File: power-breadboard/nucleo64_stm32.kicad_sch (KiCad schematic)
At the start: 29 parts, among them U5 STM32G474RBT6

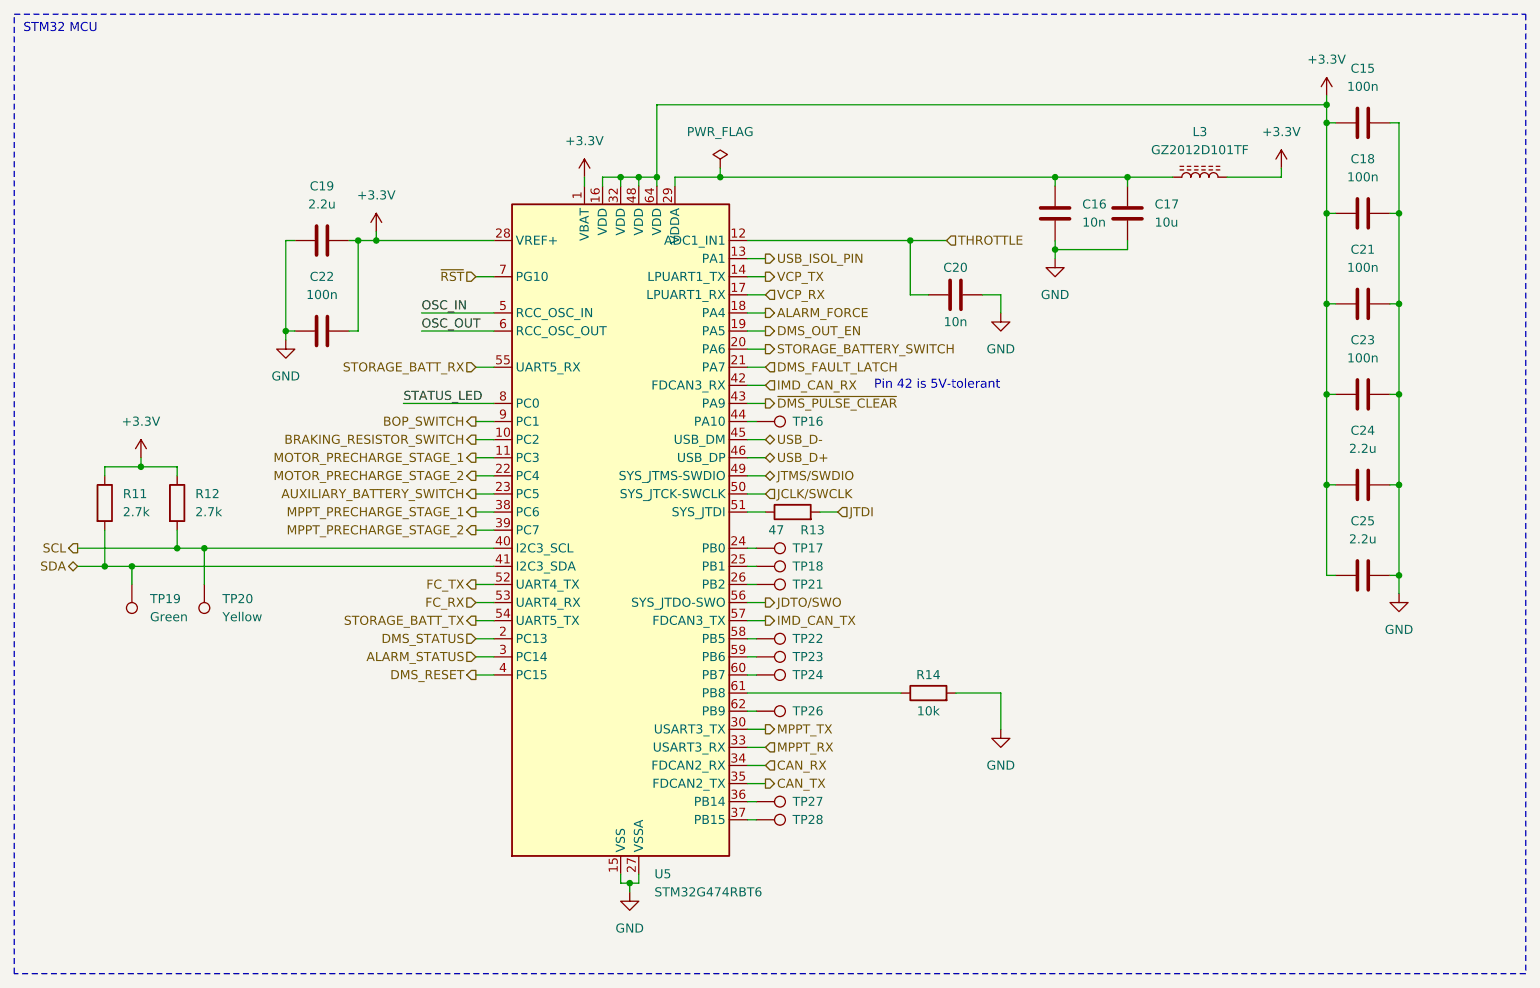
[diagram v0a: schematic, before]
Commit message: power-breadboard: add nucleo pinout connections
- Replace the schematic page with STM32 microcontroller connections.
- Update the date on all pages and some page names
- Add CN10/CN7 connectors, with the CN7 being connected through the
  T-cobbler
- Add peripheral assignation table
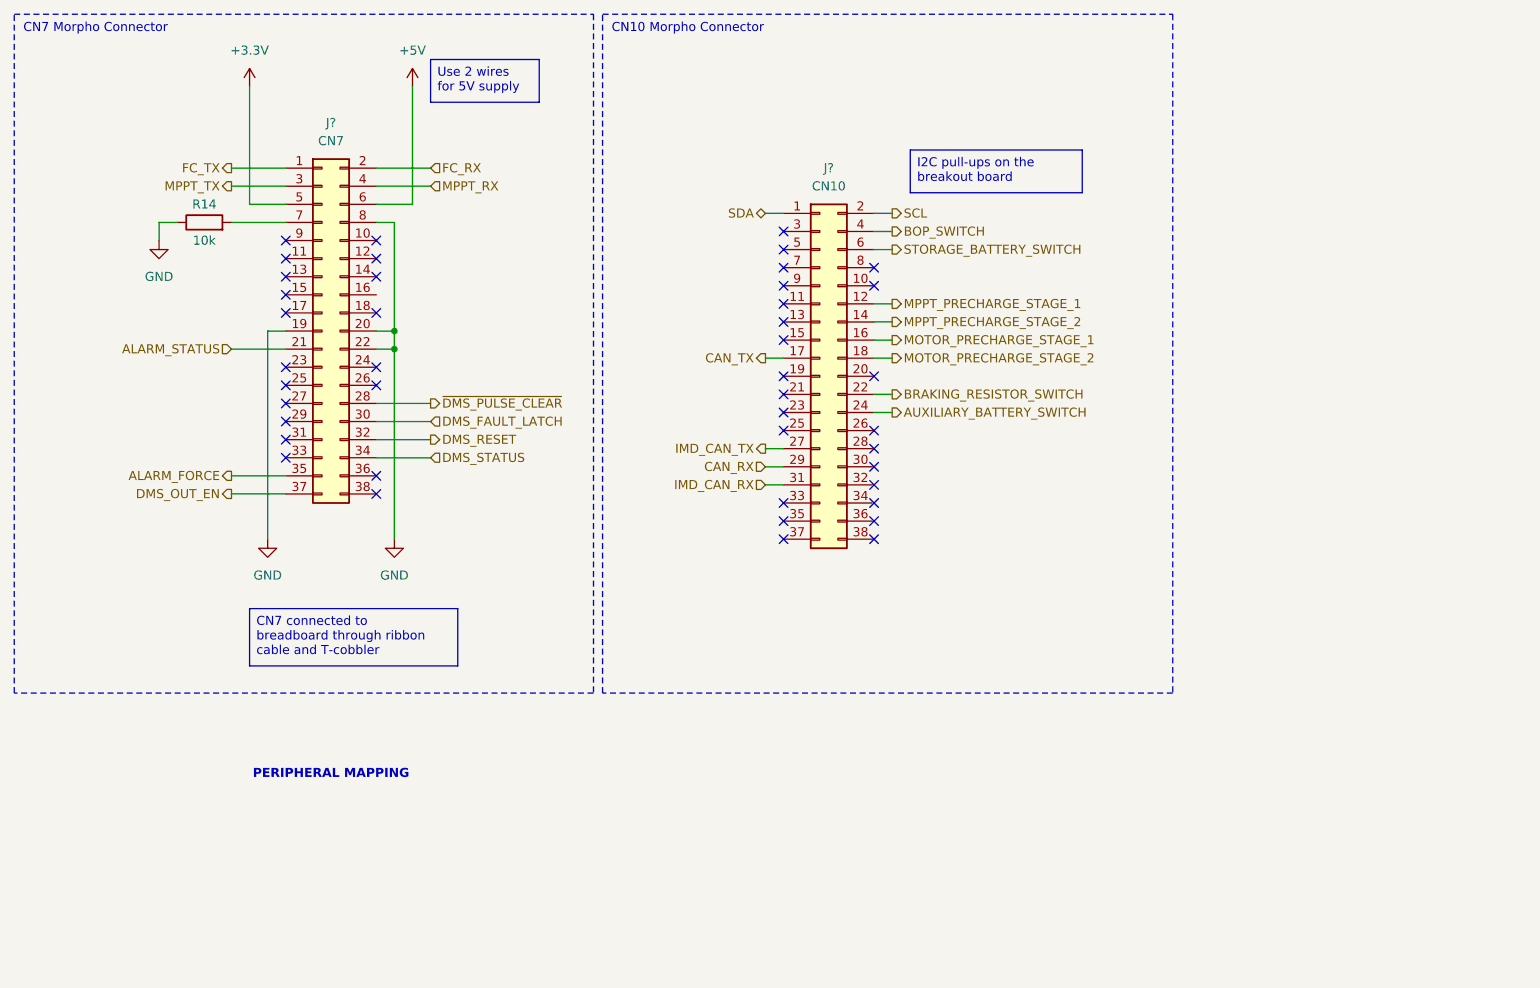
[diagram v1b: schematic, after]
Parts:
- removed C15, C18, C21, C22, C23: 100n, Capacitor_SMD:C_0402_1005Metric_Pad0.74x0.62mm_HandSolder, symbol Device:C
- removed C16, C20: 10n, Capacitor_SMD:C_0402_1005Metric_Pad0.74x0.62mm_HandSolder, symbol Device:C
- removed C17: 10u, Capacitor_SMD:C_1206_3216Metric_Pad1.33x1.80mm_HandSolder, symbol Device:C
- removed C19, C24, C25: 2.2u, Capacitor_SMD:C_0805_2012Metric_Pad1.18x1.45mm_HandSolder, symbol Device:C
- removed L3: GZ2012D101TF, Inductor_SMD:L_0805_2012Metric_Pad1.05x1.20mm_HandSolder, symbol Device:L_Ferrite
- removed R11, R12: 2.7k, Resistor_SMD:R_0603_1608Metric_Pad0.98x0.95mm_HandSolder, symbol Device:R
- removed R13: 47, Resistor_SMD:R_0603_1608Metric_Pad0.98x0.95mm_HandSolder, symbol Device:R
- removed TP16, TP17, TP18, TP21, TP22, TP23, TP24, TP26, TP27, TP28: Hole, TestPoint:TestPoint_THTPad_D2.0mm_Drill1.0mm, symbol Connector:TestPoint
- removed TP19: Green, TestPoint:TestPoint_Keystone_5005-5009_Compact, symbol Connector:TestPoint
- removed TP20: Yellow, TestPoint:TestPoint_Keystone_5005-5009_Compact, symbol Connector:TestPoint
- removed U5: STM32G474RBT6, Package_QFP:LQFP-64_10x10mm_P0.5mm, symbol MCU_ST_STM32G4:STM32G474RBTx
- added J?: CN10, symbol Connector_Generic:Conn_02x19_Odd_Even
- added J?: CN7, symbol Connector_Generic:Conn_02x19_Odd_Even
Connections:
- net +3.3V: now also J?.5 (Pin_5)
- net ALARM_FORCE: now also J?.35 (Pin_35)
- net ALARM_STATUS: now also J?.21 (Pin_21)
- net AUXILIARY_BATTERY_SWITCH: now also J?.24 (Pin_24)
- net BOP_SWITCH: now also J?.4 (Pin_4)
- net BRAKING_RESISTOR_SWITCH: now also J?.22 (Pin_22)
- net CAN_RX: now also J?.29 (Pin_29)
- net CAN_TX: now also J?.17 (Pin_17)
- net DMS_FAULT_LATCH: now also J?.30 (Pin_30)
- net DMS_OUT_EN: now also J?.37 (Pin_37)
- net DMS_RESET: now also J?.32 (Pin_32)
- net DMS_STATUS: now also J?.34 (Pin_34)
- net FC_RX: now also J?.2 (Pin_2)
- net FC_TX: now also J?.1 (Pin_1)
- net GND: now also R14.1, J?.19 (Pin_19), J?.20 (Pin_20), J?.22 (Pin_22), J?.8 (Pin_8); no longer R14.2
- net IMD_CAN_RX: now also J?.31 (Pin_31)
- net IMD_CAN_TX: now also J?.27 (Pin_27)
- net MOTOR_PRECHARGE_STAGE_1: now also J?.16 (Pin_16)
- net MOTOR_PRECHARGE_STAGE_2: now also J?.18 (Pin_18)
- net MPPT_PRECHARGE_STAGE_1: now also J?.12 (Pin_12)
- net MPPT_PRECHARGE_STAGE_2: now also J?.14 (Pin_14)
- net MPPT_RX: now also J?.4 (Pin_4)
- net MPPT_TX: now also J?.3 (Pin_3)
- net SCL: now also J?.2 (Pin_2)
- net SDA: now also J?.1 (Pin_1)
- net STORAGE_BATTERY_SWITCH: now also J?.6 (Pin_6)
- net ~{DMS_PULSE_CLEAR}: now also J?.28 (Pin_28)
- new net: J?.7 (Pin_7), R14.2
- new net +5V: J?.6 (Pin_6)
- no-connect marks 0 -> 43
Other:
- note added: "CN10 Morpho Connector"
- note added: "CN7 Morpho Connector"
- note added: "PERIPHERAL MAPPING"
- note removed: "Pin 42 is 5V-tolerant"
- note removed: "STM32 MCU"
- title: STM32 Microcontroller -> NUCLEO-G474RE I/O
- moved on the sheet: R14

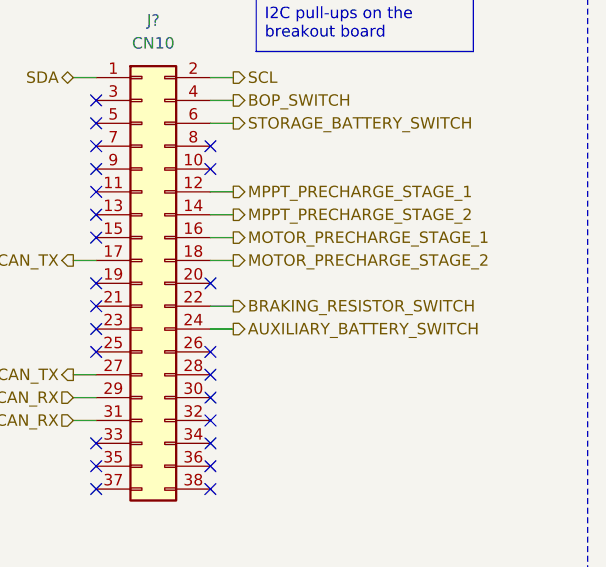
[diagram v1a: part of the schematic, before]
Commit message: power-breadboard: rename relay-board page
There are now multiple relay boards.

Also cleaned up some sheet pins on the main page.
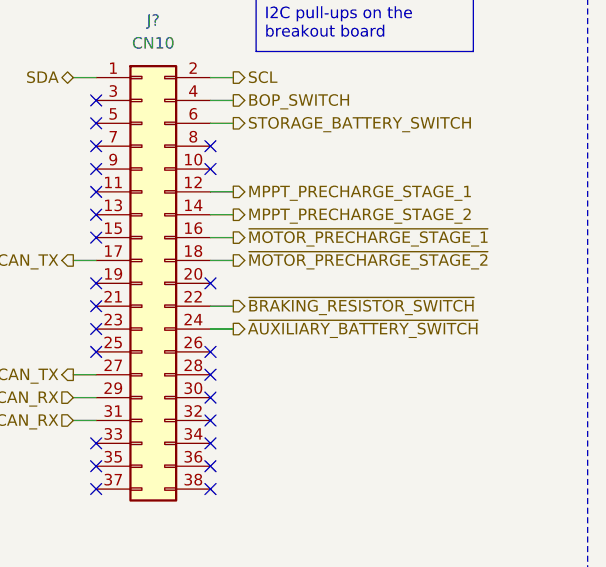
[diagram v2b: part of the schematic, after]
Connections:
- net AUXILIARY_BATTERY_SWITCH renamed ~{AUXILIARY_BATTERY_SWITCH}
- net BRAKING_RESISTOR_SWITCH renamed ~{BRAKING_RESISTOR_SWITCH}
- net MOTOR_PRECHARGE_STAGE_1 renamed ~{MOTOR_PRECHARGE_STAGE_1}
- net MOTOR_PRECHARGE_STAGE_2 renamed ~{MOTOR_PRECHARGE_STAGE_2}
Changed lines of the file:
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@@
 		)
 	)
-	(hierarchical_label "BRAKING_RESISTOR_SWITCH"
+	(hierarchical_label "~{BRAKING_RESISTOR_SWITCH}"
 		(shape output)
 		(at 135.89 66.04 0)
@@
 		)
 	)
-	(hierarchical_label "AUXILIARY_BATTERY_SWITCH"
+	(hierarchical_label "~{AUXILIARY_BATTERY_SWITCH}"
 		(shape output)
 		(at 135.89 68.58 0)
@@
 		)
 	)
-	(hierarchical_label "MOTOR_PRECHARGE_STAGE_1"
+	(hierarchical_label "~{MOTOR_PRECHARGE_STAGE_1}"
 		(shape output)
 		(at 135.89 58.42 0)
@@
 		)
 	)
-	(hierarchical_label "MOTOR_PRECHARGE_STAGE_2"
+	(hierarchical_label "~{MOTOR_PRECHARGE_STAGE_2}"
 		(shape output)
 		(at 135.89 60.96 0)
